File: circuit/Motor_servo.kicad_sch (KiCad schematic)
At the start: 42 parts, among them J17 motor1, J18 motor1, Q15 DMHT6016LFJ, Q16 DMHT6016LFJ, Q21 DMN1054UCB4, Q22 DMN1054UCB4, U17 SN74LVC1G18DSFR, U18 SN74LVC1G18DSFR, U19 DRV8701, U20 DRV8701

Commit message: AD変換の取得ができた
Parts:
- Q15, Q16: symbol robocon:DMHT6016LFJ -> robot_contest:DMHT6016LFJ
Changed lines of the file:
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@@
 	)
 	(symbol
-		(lib_id "robocon:DMHT6016LFJ")
+		(lib_id "robot_contest:DMHT6016LFJ")
 		(at 209.55 133.35 90)
 		(unit 1)
@@
 	)
 	(symbol
-		(lib_name "DMHT6016LFJ_1")
-		(lib_id "robocon:DMHT6016LFJ")
+		(lib_id "robot_contest:DMHT6016LFJ")
 		(at 209.55 55.88 90)
 		(unit 1)

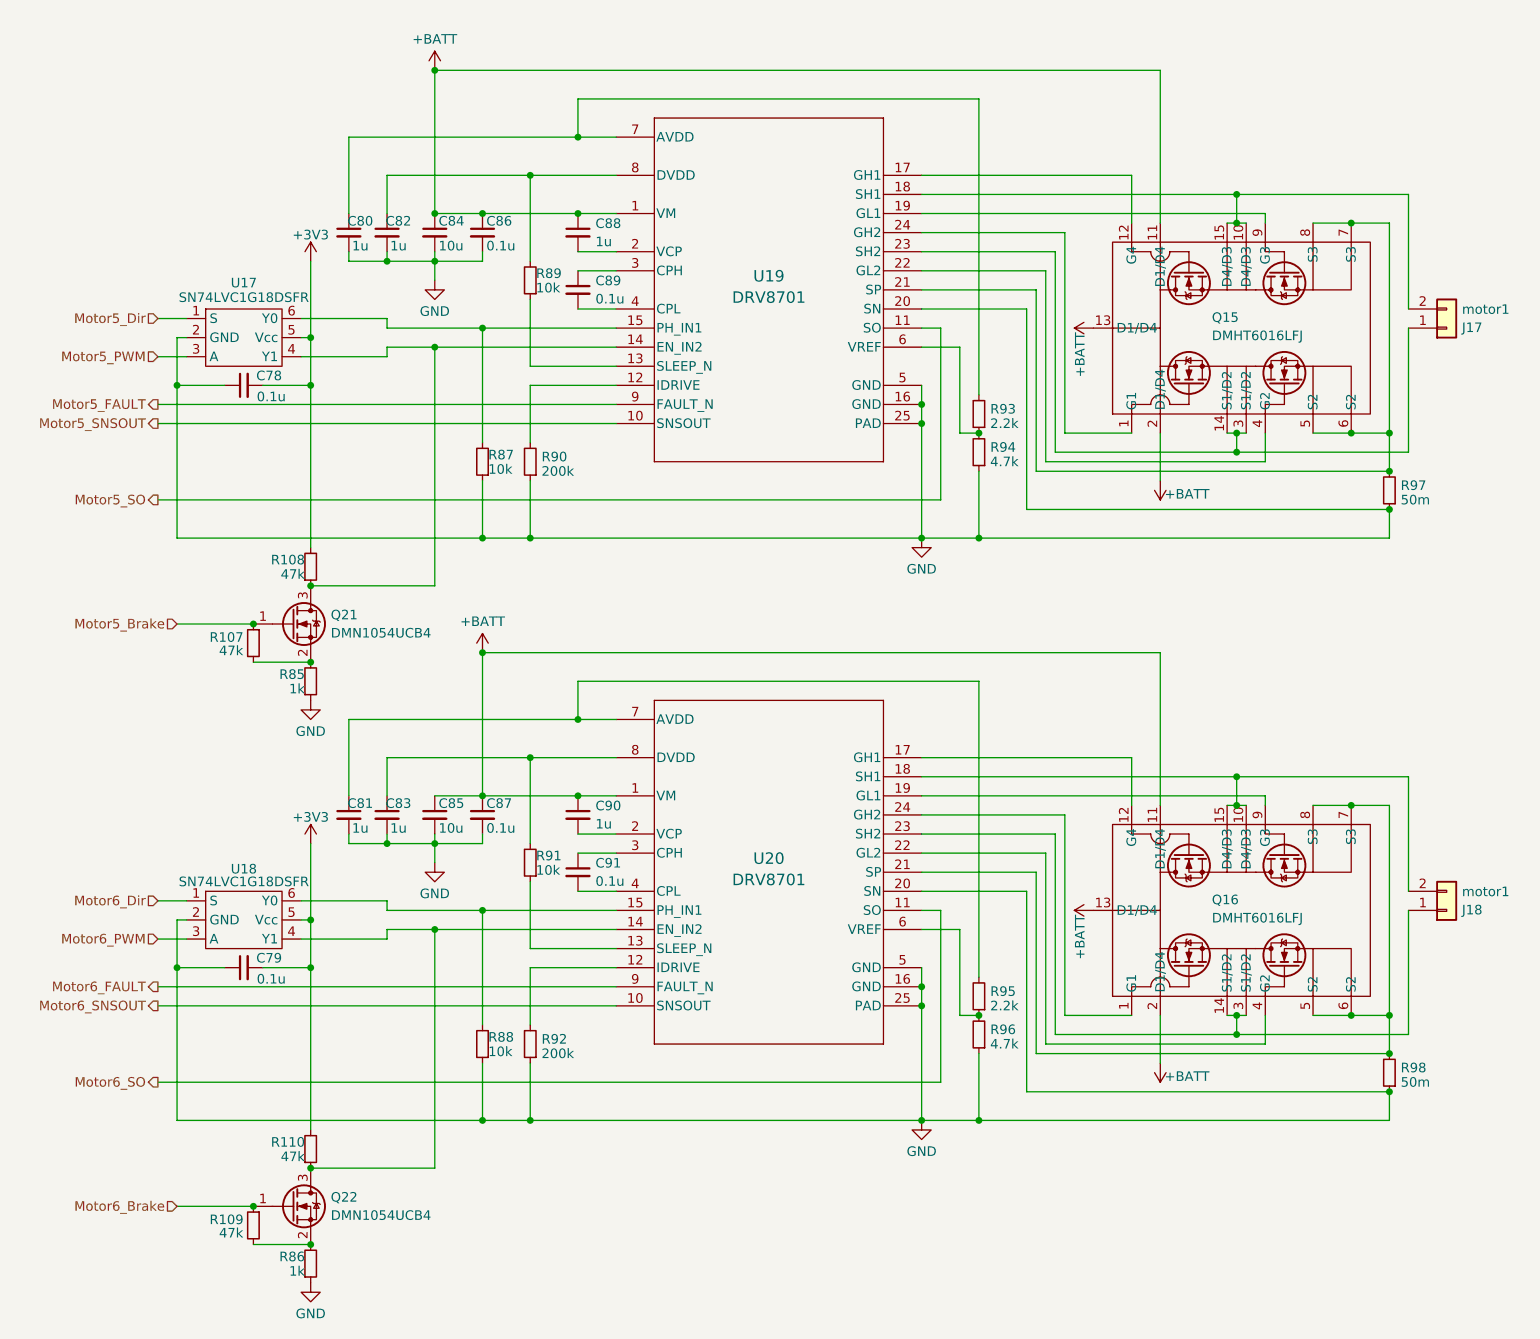
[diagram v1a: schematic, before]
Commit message: スマコンの設定変更 回路図変更
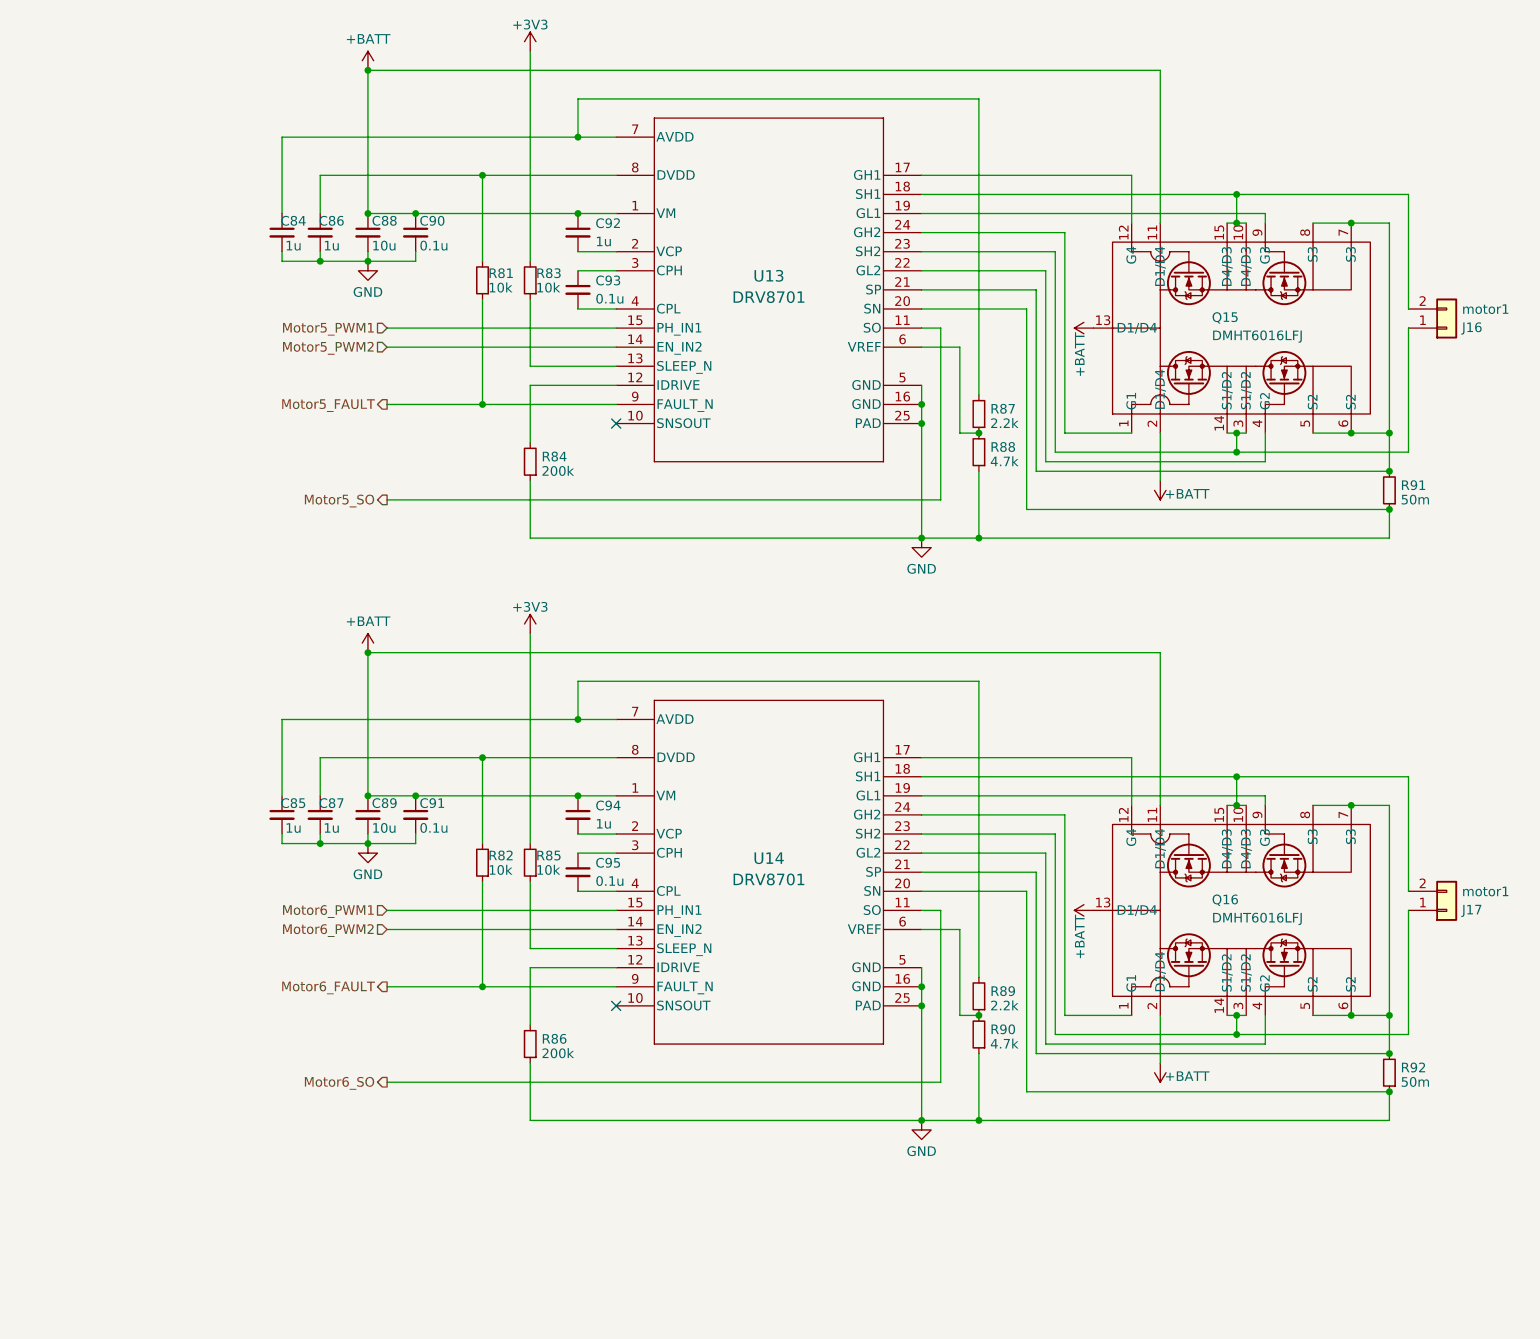
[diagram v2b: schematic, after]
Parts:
- removed C78, C79: 0.1u, Capacitor_SMD:C_0402_1005Metric, symbol Device:C_Small
- removed Q21, Q22: DMN1054UCB4, robot_contest:DMN1054UCB4, symbol Device:Q_NMOS_GSD
- removed R107, R108, R109, R110: 47k, Resistor_SMD:R_0402_1005Metric, symbol Device:R_Small
- removed R85, R86: 1k, Resistor_SMD:R_0402_1005Metric, symbol Device:R_Small
- removed R87, R88: 10k, Resistor_SMD:R_0402_1005Metric, symbol Device:R_Small
- removed U17, U18: SN74LVC1G18DSFR, robot_contest:SN74LVC1G18DSFR, symbol robocon:SN74LVC1G18
- added R81, R82: 10k, Resistor_SMD:R_0402_1005Metric, symbol Device:R_Small
- U13: renamed from U19; symbol robocon:DRV8701 -> robot_contest:DRV8701
- U14: renamed from U20; symbol robocon:DRV8701 -> robot_contest:DRV8701
- renumbered C80 to C84, C81 to C85, C82 to C86, C83 to C87, C84 to C88, C85 to C89, C86 to C90, C87 to C91, C88 to C92, C89 to C93, C90 to C94, C91 to C95, J17 to J16, J18 to J17, R89 to R83, R90 to R84, R91 to R85, R92 to R86, R93 to R87, R94 to R88, R95 to R89, R96 to R90, R97 to R91, R98 to R92
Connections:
- net +3V3: now also R83.2, R85.2
- net Motor5_FAULT: now also R81.1
- net Motor6_FAULT: now also R82.1
- net Motor6_PWM2: now reaches U14.14 (EN_IN2)
- net Motor6_PWM1: now reaches U14.15 (PH_IN1)
- net Motor5_PWM2: now reaches U13.14 (EN_IN2)
- net at C87.1, U14.8 (DVDD): now also R82.2; no longer R85.2
- net at C86.1, U13.8 (DVDD): now also R81.2; no longer R83.2
- net Motor5_PWM1: now reaches U13.15 (PH_IN1)
- net Motor5_SNSOUT: no longer names the net of U13.10 (SNSOUT)
- net Motor6_SNSOUT: no longer names the net of U14.10 (SNSOUT)
- no-connect marks 0 -> 2
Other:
- moved on the sheet: C84, C85, C86, C87, C88, C89, C90, C91
